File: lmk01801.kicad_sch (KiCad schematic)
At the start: 41 parts, among them J1001 142-0701-201, J1002 U.FL-R-SMT(10), J1003 U.FL-R-SMT(10), J1004 142-0701-201, J1005 U.FL-R-SMT(10), T1001 TCM2-43X+, T1002 TCM2-43X+, U1001 TCP-2-33W+, U1002 LMK01801BISQE/NOPB

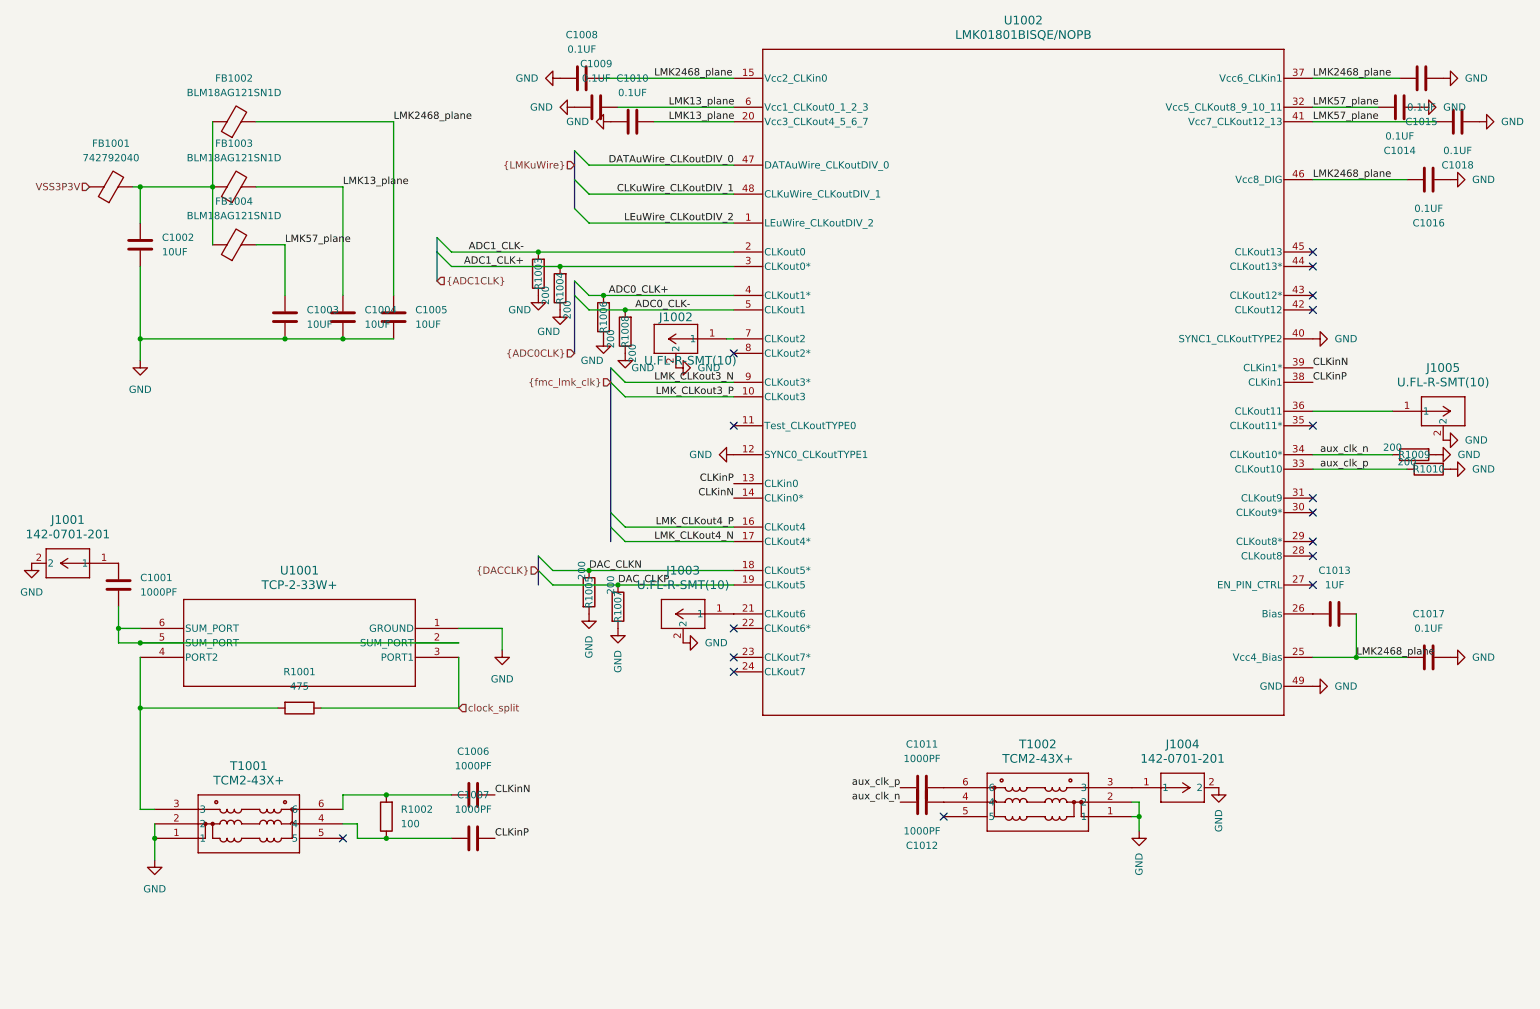
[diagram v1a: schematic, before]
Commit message: Increase layout size to accommodate more SMA connector
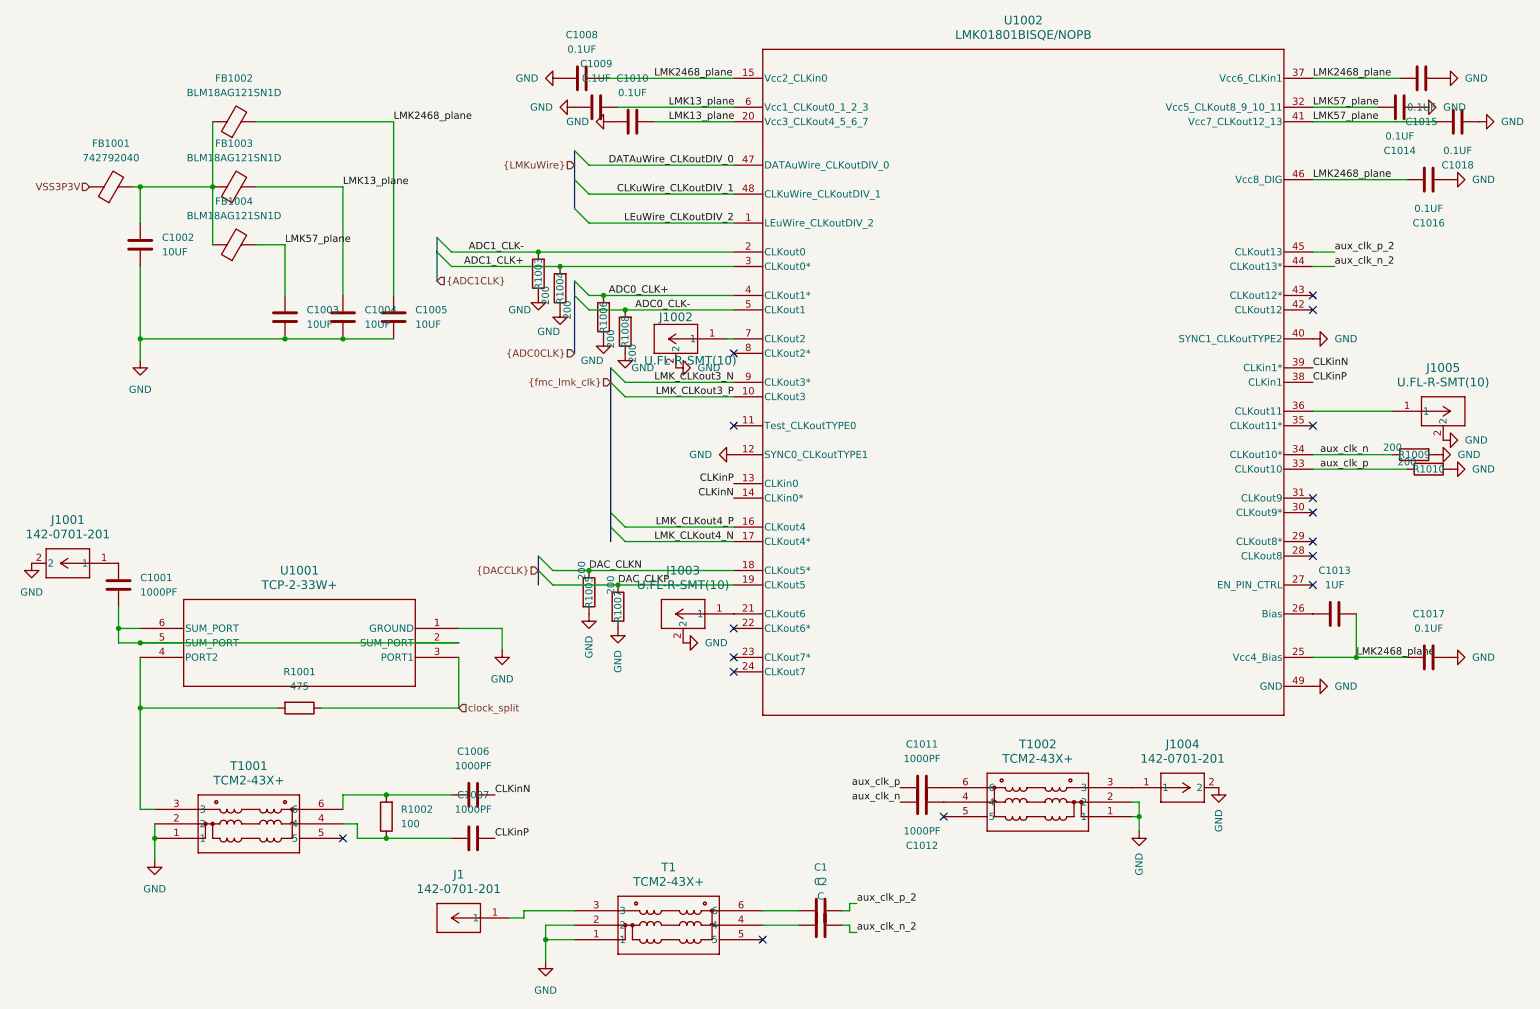
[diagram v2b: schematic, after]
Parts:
- added C1, C2: C, symbol Device:C
- added J1: 142-0701-201, CONN_142-0701-201_CIN, symbol 142_0701_201:142-0701-201
- added T1: TCM2-43X+, TCM2-43:TCM243X, symbol TCM2-43X+_digikey:TCM2-43X+
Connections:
- net GND: now also T1.1, T1.2
- net aux_clk_n_2: now reaches U1002.44 (CLKout13*)
- net aux_clk_n_2: now also C2.2
- net aux_clk_p_2: now reaches U1002.45 (CLKout13)
- net aux_clk_p_2: now also C1.2
- new net: J1.1, T1.3
- new net: C2.1, T1.4
- new net: C1.1, T1.6
- no-connect marks 17 -> 16

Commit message: update the vendores filed Update vendors  for the newly added components
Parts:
- J1: Manufacturer_Name (none) -> Cinch Connectivity Solutions Johnson; Vendor (none) -> Digikey
- T1: Manufacturer (none) -> Mini-Circuits; Vendor (none) -> Digikey
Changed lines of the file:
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@@
+			)
+		)
+		(property "Manufacturer" "Mini-Circuits"
+			(at 115.57 171.45 0)
+			(effects
+				(font
+					(size 1.27 1.27)
+				)
+				(hide yes)
+			)
+		)
+		(property "Vendor" "Digikey"
+			(at 115.57 171.45 0)
+			(effects
+				(font
+					(size 1.27 1.27)
+				)
+				(hide yes)
 			)
 		)
@@
 			)
 		)
-		(property "Description" ""
+		(property "Description" "CONN SMA JACK STR 50 OHM PCB"
 			(at 104.14 172.72 0)
 			(effects
+				(font
+					(size 1.27 1.27)
+				)
+				(hide yes)
+			)
+		)
+		(property "Manufacturer_Name" "Cinch Connectivity Solutions Johnson"
+			(at 104.14 172.72 0)
+			(effects
+				(font
+					(size 1.27 1.27)
+				)
+				(hide yes)
+			)
+		)
+		(property "Vendor" "Digikey"
+			(at 104.14 172.72 0)
+			(effects
